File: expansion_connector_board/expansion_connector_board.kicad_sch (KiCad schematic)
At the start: 12 parts, among them J1 Conn_01x04, J12 Conn_02x17_Top_Bottom, J13 Conn_01x04, J14 Conn_02x17_Top_Bottom, J2 ESP32 JTAG+UART (TE0790), J3 Conn_02x02_Odd_Even, J5 ESP32 Sensor, J6 ESP32/Peripheral UART Interfa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, U1 ESP32-WROOM-32D

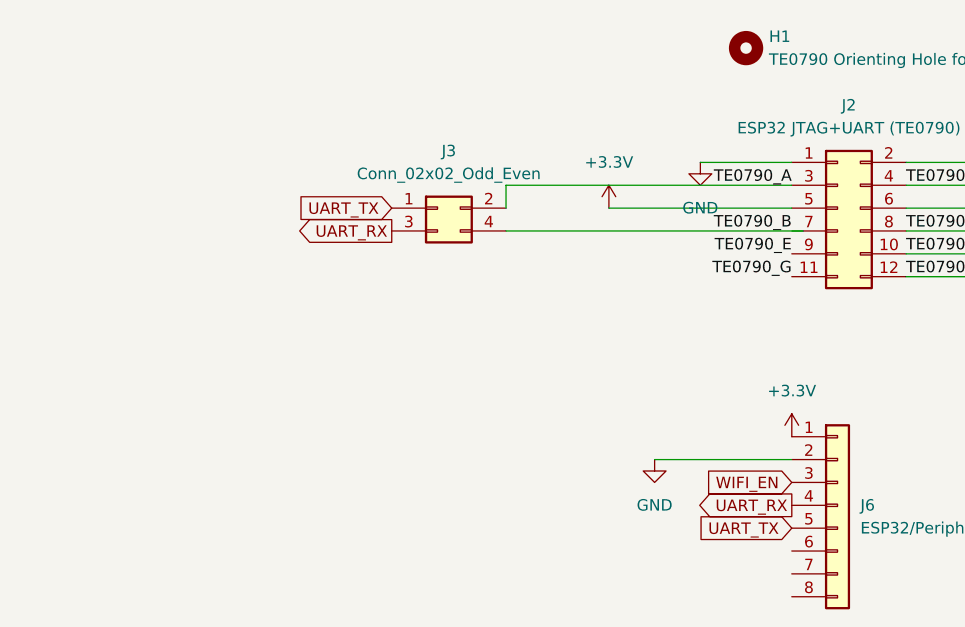
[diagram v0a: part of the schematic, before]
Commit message: add remaining connectors to bridge board
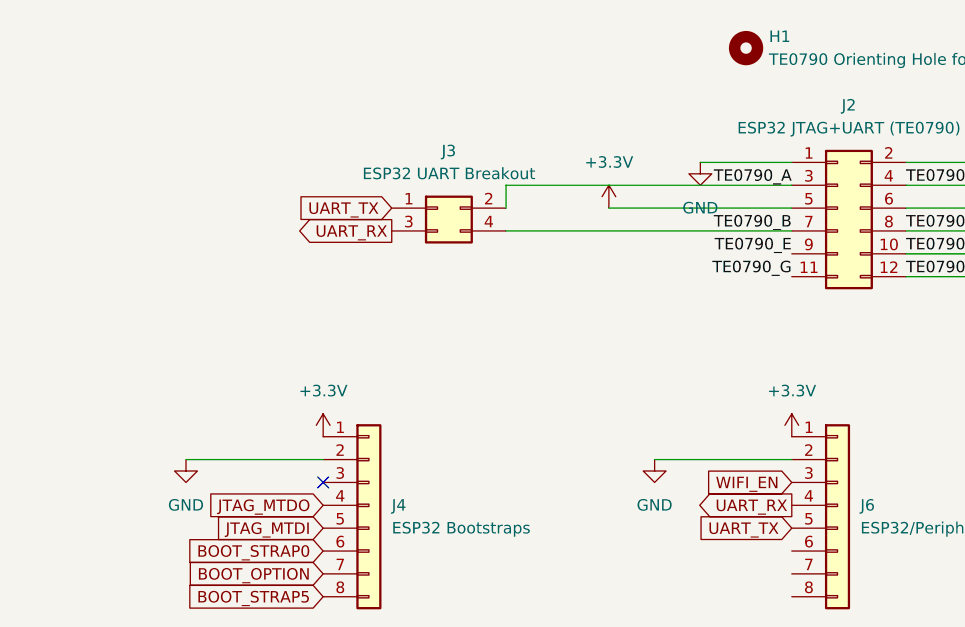
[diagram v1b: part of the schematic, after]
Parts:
- added J4: ESP32 Bootstraps, Connector_PinHeader_2.54mm:PinHeader_1x08_P2.54mm_Vertical, symbol Connector_Generic:Conn_01x08
- J3: value Conn_02x02_Odd_Even -> ESP32 UART Breakout; footprint (none) -> Connector_PinHeader_2.54mm:PinHeader_2x02_P2.54mm_Vertical
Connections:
- net +3.3V: now also J4.1 (Pin_1)
- net BOOT_OPTION: now also J4.7 (Pin_7)
- net BOOT_STRAP0: now also J4.6 (Pin_6)
- net BOOT_STRAP5: now also J4.8 (Pin_8)
- net GND: now also J4.2 (Pin_2)
- net JTAG_MTDI: now also J4.5 (Pin_5)
- net JTAG_MTDO: now also J4.4 (Pin_4)
- no-connect marks 20 -> 21
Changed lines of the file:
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@@
   (no_connect (at 251.46 111.76))
   (no_connect (at 220.98 124.46))
+  (no_connect (at 100.33 144.78))
   (no_connect (at 251.46 114.3))
   (wire (pts (xy 177.8 74.93) (xy 177.8 76.2))
@@
     (stroke (width 0) (type default))
   )
+  (wire (pts (xy 120.65 116.84) (xy 152.4 116.84))
+    (stroke (width 0) (type default))
+  )
   (wire (pts (xy 140.97 46.99) (xy 177.8 46.99))
     (stroke (width 0) (type default))
@@
     (stroke (width 0) (type default))
   )
+  (wire (pts (xy 85.09 142.24) (xy 100.33 142.24))
+    (stroke (width 0) (type default))
+  )
   (wire (pts (xy 132.08 114.3) (xy 152.4 114.3))
     (stroke (width 0) (type default))
@@
   )
   (wire (pts (xy 22.86 40.64) (xy 41.91 40.64))
-    (stroke (width 0) (type default))
-  )
-  (wire (pts (xy 120.65 116.84) (xy 153.67 116.84))
     (stroke (width 0) (type default))
   )
@@
     )
   )
+  (global_label "BOOT_STRAP5" (shape input) (at 100.33 157.48 180) (fields_autoplaced)
+    (effects (font (size 1.27 1.27)) (justify right))
+    (property "Intersheetrefs" "${INTERSHEET_REFS}" (at 84.4634 157.48 0)
+      (effects (font (size 1.27 1.27)) (justify right) hide)
+    )
+  )
   (global_label "UART_RX" (shape output) (at 107.95 116.84 180) (fields_autoplaced)
     (effects (font (size 1.27 1.27)) (justify right))
@@
     )
   )
+  (global_label "BOOT_STRAP0" (shape input) (at 100.33 152.4 180) (fields_autoplaced)
+    (effects (font (size 1.27 1.27)) (justify right))
+    (property "Intersheetrefs" "${INTERSHEET_REFS}" (at 84.4634 152.4 0)
+      (effects (font (size 1.27 1.27)) (justify right) hide)
+    )
+  )
   (global_label "WIFI_EN" (shape input) (at 220.98 83.82 180) (fields_autoplaced)
     (effects (font (size 1.27 1.27)) (justify right))
@@
     )
   )
+  (global_label "BOOT_OPTION" (shape input) (at 100.33 154.94 180) (fields_autoplaced)
+    (effects (font (size 1.27 1.27)) (justify right))
+    (property "Intersheetrefs" "${INTERSHEET_REFS}" (at 84.6447 154.94 0)
+      (effects (font (size 1.27 1.27)) (justify right) hide)
+    )
+  )
   (global_label "WIFI_EN" (shape input) (at 152.4 144.78 180) (fields_autoplaced)
     (effects (font (size 1.27 1.27)) (justify right))
@@
     )
   )
+  (global_label "JTAG_MTDO" (shape input) (at 100.33 147.32 180) (fields_autoplaced)
+    (effects (font (size 1.27 1.27)) (justify right))
+    (property "Intersheetrefs" "${INTERSHEET_REFS}" (at 87.0639 147.32 0)
+      (effects (font (size 1.27 1.27)) (justify right) hide)
+    )
+  )
+  (global_label "JTAG_MTDI" (shape input) (at 100.33 149.86 180) (fields_autoplaced)
+    (effects (font (size 1.27 1.27)) (justify right))
+    (property "Intersheetrefs" "${INTERSHEET_REFS}" (at 87.7896 149.86 0)
+      (effects (font (size 1.27 1.27)) (justify right) hide)
+    )
+  )
   (global_label "UART_TX" (shape input) (at 251.46 86.36 0) (fields_autoplaced)
     (effects (font (size 1.27 1.27)) (justify left))
@@
         (path "/5cf04621-2344-4d80-a97f-45b514527429"
           (reference "#PWR07") (unit 1)
+        )
+      )
+    )
+  )
+  (symbol (lib_id "power:+3.3V") (at 100.33 139.7 0) (unit 1)
+    (in_bom yes) (on_board yes) (dnp no) (fields_autoplaced)
+    (property "Reference" "#PWR09" (at 100.33 143.51 0)
+      (effects (font (size 1.27 1.27)) hide)
+    )
+    (property "Value" "+3.3V" (at 100.33 134.62 0)
+      (effects (font (size 1.27 1.27)))
+    )
+    (property "Footprint" "" (at 100.33 139.7 0)
+      (effects (font (size 1.27 1.27)) hide)
+    )
+    (property "Datasheet" "" (at 100.33 139.7 0)
+      (effects (font (size 1.27 1.27)) hide)
+    )
+    (pin "1")
+    (instances
+      (project "expansion_connector_board"
+        (path "/5cf04621-2344-4d80-a97f-45b514527429"
+          (reference "#PWR09") (unit 1)
         )
       )
@@
       (effects (font (size 1.27 1.27)))
     )
-    (property "Value" "Conn_02x02_Odd_Even" (at 114.3 110.49 0)
-      (effects (font (size 1.27 1.27)))
-    )
-    (property "Footprint" "" (at 113.03 114.3 0)
+    (property "Value" "ESP32 UART Breakout" (at 114.3 110.49 0)
+      (effects (font (size 1.27 1.27)))
+    )
+    (property "Footprint" "Connector_PinHeader_2.54mm:PinHeader_2x02_P2.54mm_Vertical" (at 113.03 114.3 0)
       (effects (font (size 1.27 1.27)) hide)
     )
@@
         (path "/5cf04621-2344-4d80-a97f-45b514527429"
           (reference "J3") (unit 1)
+        )
+      )
+    )
+  )
+  (symbol (lib_id "power:GND") (at 85.09 142.24 0) (unit 1)
+    (in_bom yes) (on_board yes) (dnp no) (fields_autoplaced)
+    (property "Reference" "#PWR010" (at 85.09 148.59 0)
+      (effects (font (size 1.27 1.27)) hide)
+    )
+    (property "Value" "GND" (at 85.09 147.32 0)
+      (effects (font (size 1.27 1.27)))
+    )
+    (property "Footprint" "" (at 85.09 142.24 0)
+      (effects (font (size 1.27 1.27)) hide)
+    )
+    (property "Datasheet" "" (at 85.09 142.24 0)
+      (effects (font (size 1.27 1.27)) hide)
+    )
+    (pin "1")
+    (instances
+      (project "expansion_connector_board"
+        (path "/5cf04621-2344-4d80-a97f-45b514527429"
+          (reference "#PWR010") (unit 1)
         )
       )
@@
         )
       )
+    )
+  )
+  (symbol (lib_id "Connector_Generic:Conn_01x08") (at 105.41 147.32 0) (unit 1)
+    (in_bom yes) (on_board yes) (dnp no) (fields_autoplaced)
+    (property "Reference" "J4" (at 107.95 147.32 0)
+      (effects (font (size 1.27 1.27)) (justify left))
+    )
+    (property "Value" "ESP32 Bootstraps" (at 107.95 149.86 0)
+      (effects (font (size 1.27 1.27)) (justify left))
+    )
+    (property "Footprint" "Connector_PinHeader_2.54mm:PinHeader_1x08_P2.54mm_Vertical" (at 105.41 147.32 0)
+      (effects (font (size 1.27 1.27)) hide)
+    )
+    (property "Datasheet" "~" (at 105.41 147.32 0)
+      (effects (font (size 1.27 1.27)) hide)
+    )
+    (pin "8")
+    (pin "1")
+    (pin "7")
+    (pin "2")
+    (pin "4")
+    (pin "5")
+    (pin "3")
+    (pin "6")
+    (instances
+      (project "expansion_connector_board"
+        (path "/5cf04621-2344-4d80-a97f-45b514527429"
+          (reference "J4") (unit 1)
+        )
+      )

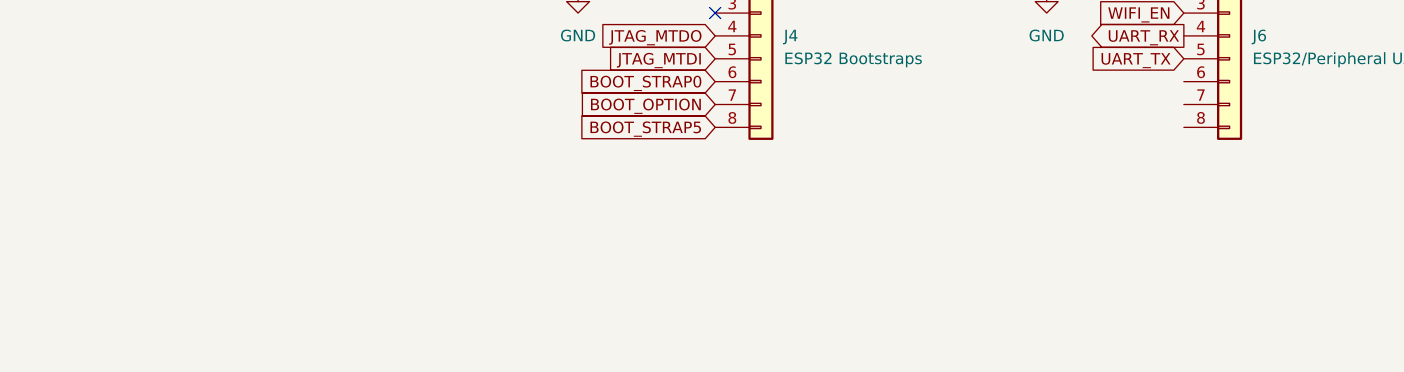
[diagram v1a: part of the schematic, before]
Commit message: add MEGA65 and open hardware logos etc
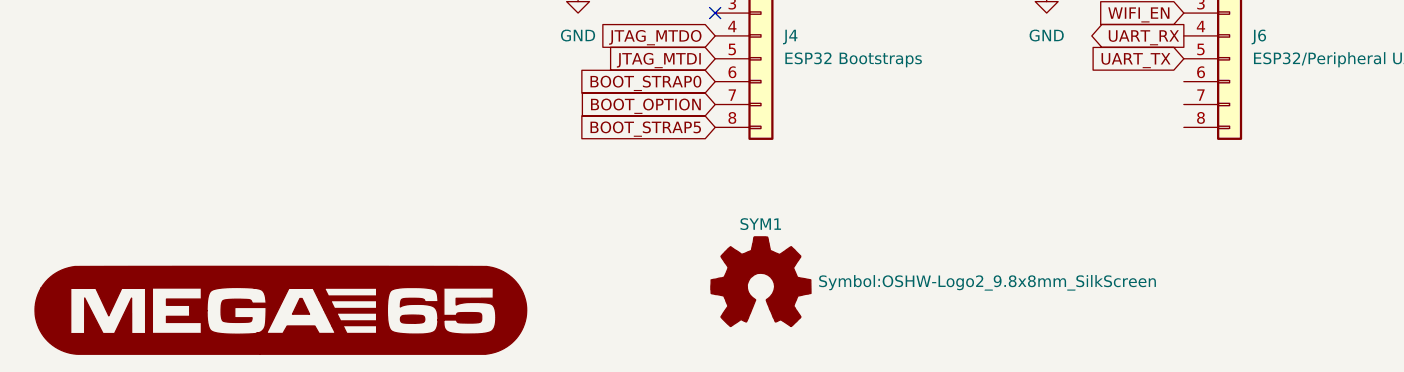
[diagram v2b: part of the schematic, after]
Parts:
- added G1: LOGO, 00Project:MEGA65-logo, symbol snapeda:LOGO
- added SYM1: Logo_Open_Hardware_Small, Symbol:OSHW-Logo2_9.8x8mm_SilkScreen, symbol Graphic:Logo_Open_Hardware_Small
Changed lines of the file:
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@@
+    )
+  )
+  (symbol (lib_id "Graphic:Logo_Open_Hardware_Small") (at 105.41 175.26 0) (unit 1)
+    (in_bom no) (on_board yes) (dnp no) (fields_autoplaced)
+    (property "Reference" "SYM1" (at 105.41 168.275 0)
+      (effects (font (size 1.27 1.27)))
+    )
+    (property "Value" "Logo_Open_Hardware_Small" (at 105.41 180.975 0)
+      (effects (font (size 1.27 1.27)) hide)
+    )
+    (property "Footprint" "Symbol:OSHW-Logo2_9.8x8mm_SilkScreen" (at 111.76 174.625 0)
+      (effects (font (size 1.27 1.27)) (justify left))
+    )
+    (property "Datasheet" "~" (at 105.41 175.26 0)
+      (effects (font (size 1.27 1.27)) hide)
+    )
+    (property "Sim.Enable" "0" (at 105.41 175.26 0)
+      (effects (font (size 1.27 1.27)) hide)
+    )
+    (instances
+      (project "expansion_connector_board"
+        (path "/5cf04621-2344-4d80-a97f-45b514527429"
+          (reference "SYM1") (unit 1)
+        )
+      )
     )
   )
@@
         )
       )
+    )
+  )
+  (symbol (lib_id "snapeda:LOGO") (at 52.07 177.8 0) (unit 1)
+    (in_bom yes) (on_board yes) (dnp no) (fields_autoplaced)
+    (property "Reference" "G1" (at 52.07 173.5526 0)
+      (effects (font (size 1.27 1.27)) hide)
+    )
+    (property "Value" "LOGO" (at 52.07 182.0474 0)
+      (effects (font (size 1.27 1.27)) hide)
+    )
+    (property "Footprint" "00Project:MEGA65-logo" (at 52.07 177.8 0)
+      (effects (font (size 1.27 1.27)) hide)
+    )
+    (property "Datasheet" "" (at 52.07 177.8 0)
+      (effects (font (size 1.27 1.27)) hide)
+    )
+    (instances
+      (project "expansion_connector_board"
+        (path "/5cf04621-2344-4d80-a97f-45b514527429"
+          (reference "G1") (unit 1)
+        )
+      )

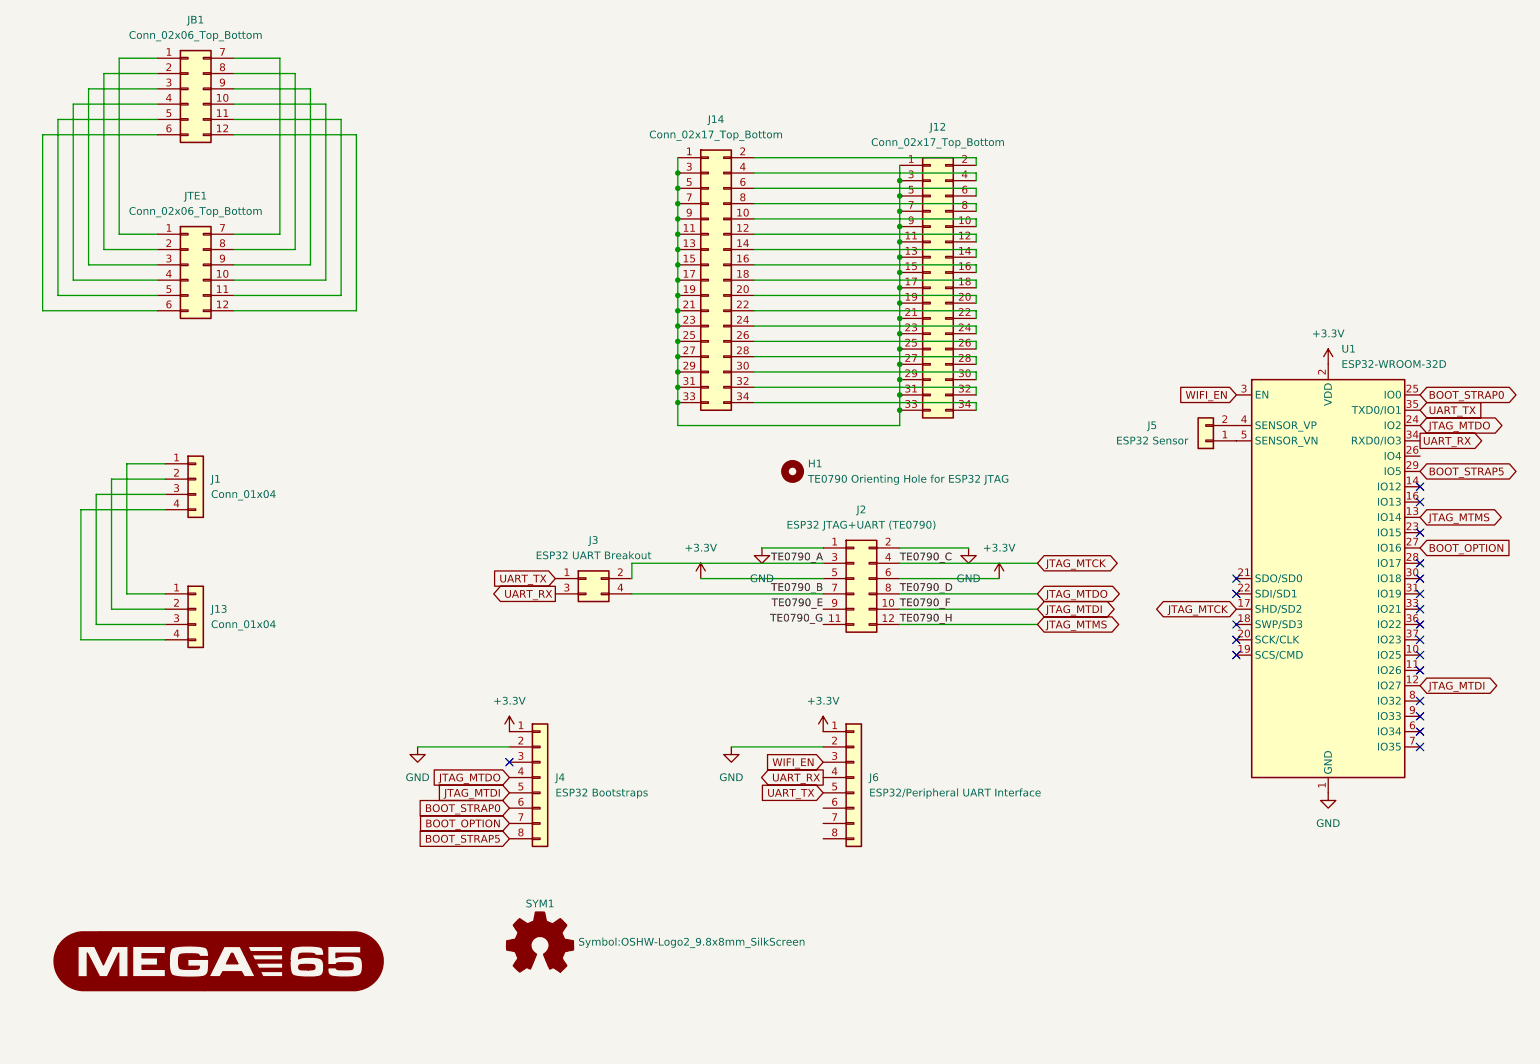
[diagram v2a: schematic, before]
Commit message: add audio J19 pickup header
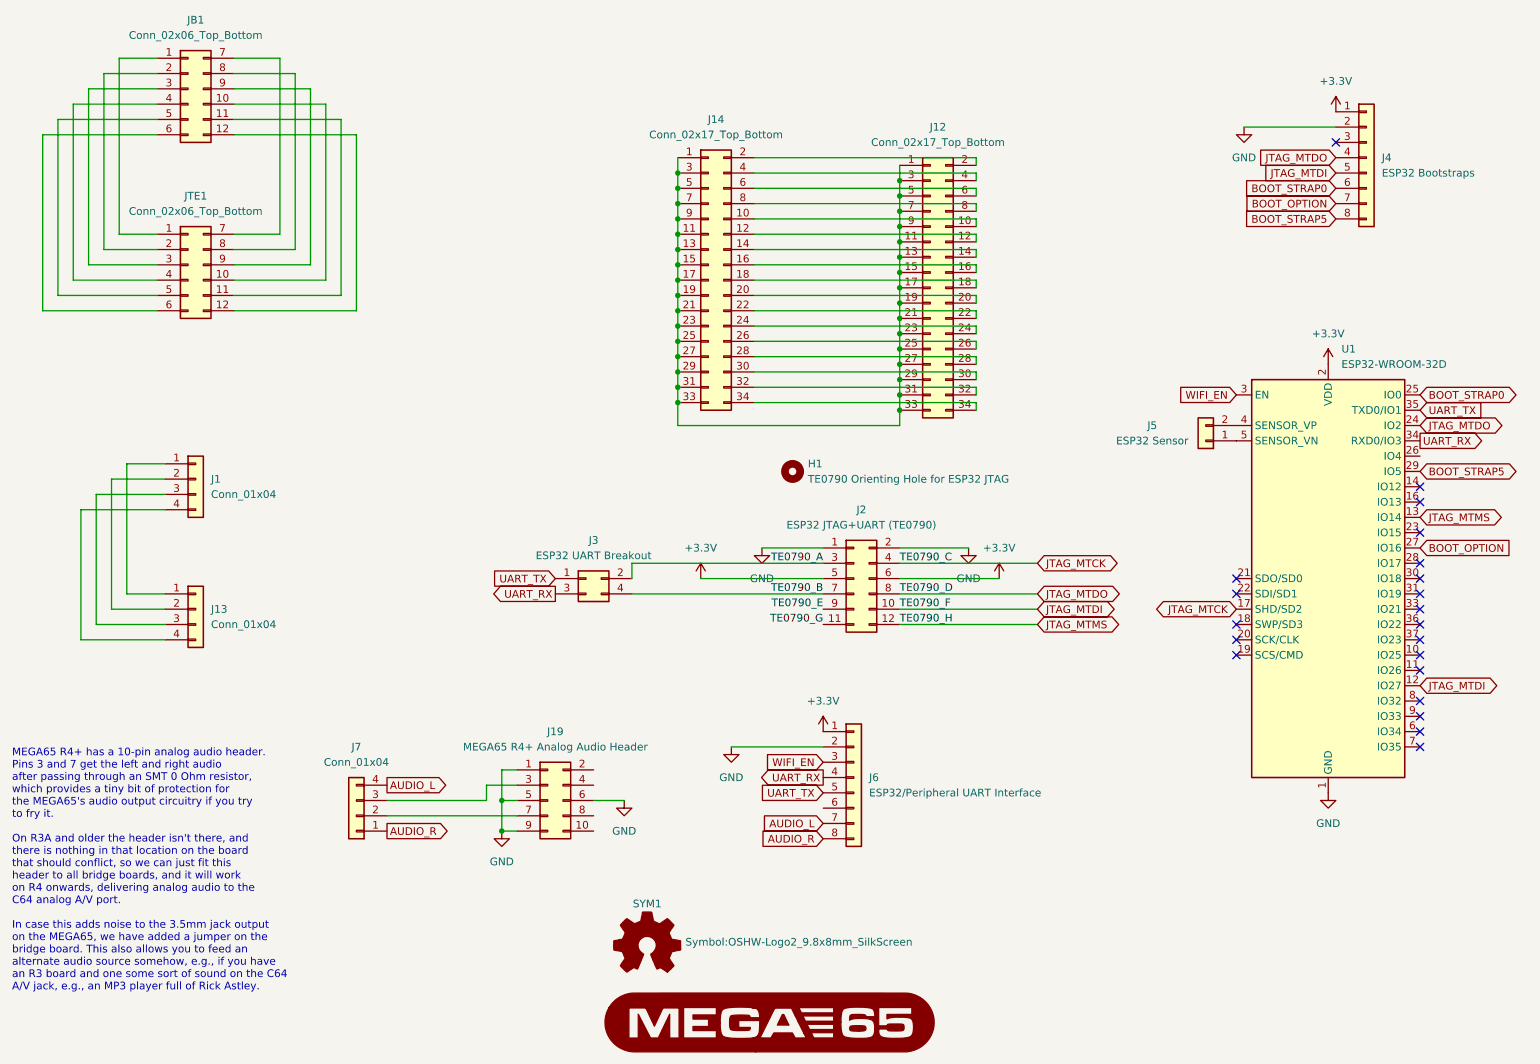
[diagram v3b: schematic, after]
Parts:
- added J19: MEGA65 R4+ Analog Audio Header, Connector_PinHeader_2.54mm:PinHeader_2x05_P2.54mm_Vertical, symbol Connector_Generic:Conn_02x05_Odd_Even
- added J7: Conn_01x04, Connector_PinHeader_2.54mm:PinHeader_1x04_P2.54mm_Vertical, symbol Connector_Generic:Conn_01x04
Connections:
- net GND: now also J19.1 (Pin_1), J19.5 (Pin_5), J19.6 (Pin_6), J19.9 (Pin_9)
- net AUDIO_L: now reaches J6.7 (Pin_7)
- net AUDIO_L: now also J7.4 (Pin_4)
- net AUDIO_R: now reaches J6.8 (Pin_8)
- net AUDIO_R: now also J7.1 (Pin_1)
- new net: J19.7 (Pin_7), J7.2 (Pin_2)
- new net: J19.3 (Pin_3), J7.3 (Pin_3)
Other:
- note added: "MEGA65 R4+ has a 10-pin analog audio header. Pins 3 and 7 get the left and right audio after passing through an SMT 0 Ohm resistor, which provides a tiny bit of protection for the MEGA65's audio output circuitry if you try to fry it. On R3A and older the header isn't there, and there is nothing in that location on the board that should conflict, so we can just fit this header to all bridge boards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"
- moved on the sheet: J4, SYM1
